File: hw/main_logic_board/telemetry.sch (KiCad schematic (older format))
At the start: 1 part

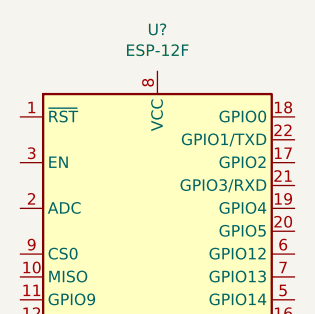
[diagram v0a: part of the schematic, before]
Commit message: Finish initial power schematics, swap some footprints for visualization in pcb view
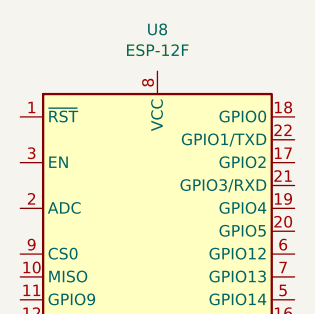
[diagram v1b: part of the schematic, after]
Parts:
- gave numbers to parts that had none: 1
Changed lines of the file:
@@
 $EndDescr
 $Comp
-L RF_Module:ESP-12F U?
+L RF_Module:ESP-12F U8
 U 1 1 5EA6AEF3
 P 6400 3200
-F 0 "U?" H 6400 4181 50  0000 C CNN
+F 0 "U8" H 6400 4181 50  0000 C CNN
 F 1 "ESP-12F" H 6400 4090 50  0000 C CNN
 F 2 "RF_Module:ESP-12E" H 6400 3200 50  0001 C CNN

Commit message: Finish prelim schematic + PCB component placement
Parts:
- added C23: 10uF, Capacitor_SMD:C_0805_2012Metric, symbol Device:C_Small
- added D5: RED, Diode_SMD:D_0805_2012Metric, symbol Device:LED
- added R10, R6, R8, R9: 10K, Resistor_SMD:R_0805_2012Metric, symbol Device:R_Small_US
- added R7: 1K, Resistor_SMD:R_0805_2012Metric, symbol Device:R_Small_US
- added SW1: ESP_RESET, Button_Switch_SMD:SW_SPST_B3U-1000P, symbol Switch:SW_Push
- added SW2: ESP_GPIO0, Button_Switch_SMD:SW_SPST_B3U-1000P, symbol Switch:SW_Push
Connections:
- net RST_N: now reaches U8.1 (~RST)
- net RST_N: now also R6.2, SW1.2
- net TELEM_MISO: now reaches U8.10 (MISO)
- net TELEM_MOSI: now reaches U8.13 (MOSI)
- net TELEM_SCLK: now reaches U8.14 (SCLK)
- net GND: now reaches U8.15 (GND)
- net GND: now also C23.2, R9.2, SW1.1, SW2.1
- net GPIO15: now reaches U8.16 (GPIO15)
- net GPIO15: now also R9.1
- net GPIO2: now reaches U8.17 (GPIO2)
- net GPIO2: now also R8.2
- net GPIO0: now reaches U8.18 (GPIO0)
- net GPIO0: now also R7.2, SW2.2
- net TELEM_RXD: now reaches U8.21 (GPIO3/RXD)
- net TELEM_TXD: now reaches U8.22 (GPIO1/TXD)
- net CH_PD: now reaches U8.3 (EN)
- net CH_PD: now also R10.2
- net +3V3: now reaches U8.8 (VCC)
- net +3V3: now also C23.1, D5.2 (A), R10.1, R6.1, R8.1
- net TELEM_CS_N: now reaches U8.9 (CS0)
- new net: D5.1 (K), R7.1
- no-connect marks 0 -> 9
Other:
- moved on the sheet: U8

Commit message: Adding BOM information
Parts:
- SW1, SW2: Digikey (none) -> https://www.digikey.ca/product-detail/en/omron-electronics-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
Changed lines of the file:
@@
 F 1 "ESP_RESET" V 1505 2452 50  0000 R CNN
 F 2 "Button_Switch_SMD:SW_SPST_B3U-1000P" H 1550 2700 50  0001 C CNN
-F 3 "https://www.digikey.ca/product-detail/en/omron-electronics-inc-emc-div/B3U-1000P/SW1020CT-ND/1534357" H 1550 2700 50  0001 C CNN
+F 3 "~" H 1550 2700 50  0001 C CNN
+F 4 "https://www.digikey.ca/product-detail/en/omron-electronics-inc-emc-div/B3U-1000P/SW1020CT-ND/1534357" H 1550 2500 50  0001 C CNN "Digikey"
 	1    1550 2500
 	0    -1   -1   0
@@
 F 1 "ESP_GPIO0" V 2055 2952 50  0000 R CNN
 F 2 "Button_Switch_SMD:SW_SPST_B3U-1000P" H 2100 3200 50  0001 C CNN
-F 3 "https://www.digikey.ca/product-detail/en/omron-electronics-inc-emc-div/B3U-1000P/SW1020CT-ND/1534357" H 2100 3200 50  0001 C CNN
+F 3 "~" H 2100 3200 50  0001 C CNN
+F 4 "https://www.digikey.ca/product-detail/en/omron-electronics-inc-emc-div/B3U-1000P/SW1020CT-ND/1534357" H 2100 3000 50  0001 C CNN "Digikey"
 	1    2100 3000
 	0    -1   -1   0

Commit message: Update repo with latest local
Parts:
- U8: Digikey (none) -> https://www.digikey.ca/product-detail/en/adafruit-industrie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
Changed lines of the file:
@@
 F 1 "ESP_RESET" V 1505 2452 50  0000 R CNN
 F 2 "Button_Switch_SMD:SW_SPST_B3U-1000P" H 1550 2700 50  0001 C CNN
-F 3 "~" H 1550 2700 50  0001 C CNN
+F 3 "https://omronfs.omron.com/en_US/ecb/products/pdf/en-b3u.pdf" H 1550 2700 50  0001 C CNN
 F 4 "https://www.digikey.ca/product-detail/en/omron-electronics-inc-emc-div/B3U-1000P/SW1020CT-ND/1534357" H 1550 2500 50  0001 C CNN "Digikey"
 	1    1550 2500
@@
 F 2 "RF_Module:ESP-12E" H 6550 4250 50  0001 C CNN
 F 3 "http://wiki.ai-thinker.com/_media/esp8266/esp8266_series_modules_user_manual_v1.1.pdf" H 6200 4350 50  0001 C CNN
+F 4 "https://www.digikey.ca/product-detail/en/adafruit-industries-llc/2491/1528-1438-ND/5761206" H 6550 4250 50  0001 C CNN "Digikey"
 	1    6550 4250
 	1    0    0    -1
@@
 F 1 "ESP_GPIO0" V 2055 2952 50  0000 R CNN
 F 2 "Button_Switch_SMD:SW_SPST_B3U-1000P" H 2100 3200 50  0001 C CNN
-F 3 "~" H 2100 3200 50  0001 C CNN
+F 3 "https://omronfs.omron.com/en_US/ecb/products/pdf/en-b3u.pdf" H 2100 3200 50  0001 C CNN
 F 4 "https://www.digikey.ca/product-detail/en/omron-electronics-inc-emc-div/B3U-1000P/SW1020CT-ND/1534357" H 2100 3000 50  0001 C CNN "Digikey"
 	1    2100 3000
